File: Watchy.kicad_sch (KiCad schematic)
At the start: 73 parts, among them J1 FPC24(0.5MM), J2 USB_C_Receptacle_USB2.0, J3 Battery, M1 Vibration_Motor, Q1 AO3400A, Q2 UMH3N, Q4 CJ2301, Q5 S8050, SW1 BTN, SW2 BTN, SW3 BTN, SW4 BTN, U1 ESP32-PICO-D4, U2 ME6211C33M5G-N, U3 CP2102, U4 BMA423, U5 TP4054, U6 PCF8563BS, Y1 32.768KHz

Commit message: fix: inconsistent and missing footprints
May have broken something.
Also updated the PCB with the new footprints.
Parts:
- C12, C3, C4: footprint Capacitors_SMD:C_0805 -> Watchy:C_0805
- D1, D2, D3, D4: footprint Diodes_SMD:D_SOD-123 -> Watchy:D_SOD-123
- D5: footprint LEDs:LED_0603 -> Watchy:LED_0603
- D6: footprint Diodes_SMD:D_SOD-123F -> Watchy:D_SOD-123
- L1: footprint Inductors:Inductor_Taiyo-Yuden_NR-40xx -> Inductor_SMD:L_Taiyo-Yuden_NR-40xx
- Q1, Q4, Q5: footprint TO_SOT_Packages_SMD:SOT-23 -> Watchy:SOT-23
- Q2: footprint TO_SOT_Packages_SMD:SOT-363_SC-70-6 -> Package_TO_SOT_SMD:SOT-363_SC-70-6
- R1, R10, R12, R13, R14, R15, R16, R17, R2, R3, R4, R5, R6, R7, R8, R9: footprint Resistors_SMD:R_0402 -> Watchy:R_0402
- U1: footprint Housings_DFN_QFN:QFN-48-1EP_7x7mm_Pitch0.5mm -> Package_DFN_QFN:QFN-48-1EP_7x7mm_P0.5mm_EP5.15x5.15mm
- U2: footprint TO_SOT_Packages_SMD:SOT-23-5 -> Watchy:SOT-23-5
- U4: footprint Housings_LGA:LGA-12_2x2mm_Pitch0.5mm -> Package_LGA:LGA-12_2x2mm_P0.5mm
- U5: footprint TO_SOT_Packages_SMD:SOT-23-5 -> Package_TO_SOT_SMD:SOT-23-5
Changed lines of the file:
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@@
       (effects (font (size 1.27 1.27)))
     )
-    (property "Footprint" "Resistors_SMD:R_0402" (at 17.399 20.574 90)
+    (property "Footprint" "Watchy:R_0402" (at 17.399 20.574 90)
       (effects (font (size 1.27 1.27)) hide)
     )
@@
       (effects (font (size 1.27 1.27)))
     )
-    (property "Footprint" "Resistors_SMD:R_0402" (at 85.09 122.174 90)
+    (property "Footprint" "Watchy:R_0402" (at 85.09 122.174 90)
       (effects (font (size 1.27 1.27)) hide)
     )
@@
       (effects (font (size 1.27 1.27)))
     )
-    (property "Footprint" "Resistors_SMD:R_0402" (at 85.09 129.794 90)
+    (property "Footprint" "Watchy:R_0402" (at 85.09 129.794 90)
       (effects (font (size 1.27 1.27)) hide)
     )
@@
       (effects (font (size 1.27 1.27)) (justify left))
     )
-    (property "Footprint" "TO_SOT_Packages_SMD:SOT-23-5" (at 51.562 113.284 0)
+    (property "Footprint" "Watchy:SOT-23-5" (at 51.562 113.284 0)
       (effects (font (size 1.27 1.27) italic) hide)
     )
@@
       (effects (font (size 1.27 1.27)) (justify left))
     )
-    (property "Footprint" "TO_SOT_Packages_SMD:SOT-23" (at 30.734 116.459 0)
+    (property "Footprint" "Watchy:SOT-23" (at 30.734 116.459 0)
       (effects (font (size 1.27 1.27) italic) (justify left) hide)
     )
@@
       (effects (font (size 1.27 1.27)))
     )
-    (property "Footprint" "Resistors_SMD:R_0402" (at 27.051 130.429 90)
+    (property "Footprint" "Watchy:R_0402" (at 27.051 130.429 90)
       (effects (font (size 1.27 1.27)) hide)
     )
@@
       (effects (font (size 1.27 1.27)))
     )
-    (property "Footprint" "Diodes_SMD:D_SOD-123" (at 32.639 126.619 0)
+    (property "Footprint" "Watchy:D_SOD-123" (at 32.639 126.619 0)
       (effects (font (size 1.27 1.27)) hide)
     )
@@
       (effects (font (size 1.27 1.27)) (justify left))
     )
-    (property "Footprint" "Capacitors_SMD:C_0805" (at 65.9892 134.112 0)
-      (effects (font (size 1.27 1.27)) hide)
-    )
-    (property "Datasheet" "" (at 65.024 130.302 0)
+    (property "Footprint" "Watchy:C_0805" (at 65.9892 134.112 0)
+      (effects (font (size 1.27 1.27)) hide)
+    )
+    (property "Datasheet" "~" (at 65.024 130.302 0)
       (effects (font (size 1.27 1.27)) hide)
     )
@@
       (effects (font (size 1.524 1.524)))
     )
-    (property "Footprint" "TO_SOT_Packages_SMD:SOT-23-5" (at 23.876 157.48 0)
+    (property "Footprint" "Package_TO_SOT_SMD:SOT-23-5" (at 23.876 157.48 0)
       (effects (font (size 1.524 1.524)) hide)
     )
@@
       (effects (font (size 1.27 1.27)))
     )
-    (property "Footprint" "Resistors_SMD:R_0402" (at 42.164 153.797 90)
+    (property "Footprint" "Watchy:R_0402" (at 42.164 153.797 90)
       (effects (font (size 1.27 1.27)) hide)
     )
@@
       (effects (font (size 1.27 1.27)))
     )
-    (property "Footprint" "LEDs:LED_0603" (at 46.482 151.765 0)
-      (effects (font (size 1.27 1.27)) hide)
-    )
-    (property "Datasheet" "" (at 46.482 151.765 0)
+    (property "Footprint" "Watchy:LED_0603" (at 46.482 151.765 0)
+      (effects (font (size 1.27 1.27)) hide)
+    )
+    (property "Datasheet" "~" (at 46.482 151.765 0)
       (effects (font (size 1.27 1.27)) hide)
     )
@@
       (effects (font (size 1.27 1.27)))
     )
-    (property "Footprint" "Resistors_SMD:R_0402" (at 19.304 159.385 90)
+    (property "Footprint" "Watchy:R_0402" (at 19.304 159.385 90)
       (effects (font (size 1.27 1.27)) hide)
     )
@@
       (effects (font (size 1.27 1.27)) (justify left))
     )
-    (property "Footprint" "Resistors_SMD:R_0402" (at 142.621 32.512 90)
+    (property "Footprint" "Watchy:R_0402" (at 142.621 32.512 90)
       (effects (font (size 1.27 1.27)) hide)
     )
@@
       (effects (font (size 1.27 1.27)) (justify left))
     )
-    (property "Footprint" "Resistors_SMD:R_0402" (at 142.621 50.292 90)
+    (property "Footprint" "Watchy:R_0402" (at 142.621 50.292 90)
       (effects (font (size 1.27 1.27)) hide)
     )
@@
       (effects (font (size 1.27 1.27)) (justify left))
     )
-    (property "Footprint" "Resistors_SMD:R_0402" (at 142.621 68.072 90)
+    (property "Footprint" "Watchy:R_0402" (at 142.621 68.072 90)
       (effects (font (size 1.27 1.27)) hide)
     )
@@
       (effects (font (size 1.27 1.27)) (justify left))
     )
-    (property "Footprint" "Resistors_SMD:R_0402" (at 142.621 85.852 90)
+    (property "Footprint" "Watchy:R_0402" (at 142.621 85.852 90)
       (effects (font (size 1.27 1.27)) hide)
     )
@@
       (effects (font (size 1.27 1.27)) (justify left))
     )
-    (property "Footprint" "Resistors_SMD:R_0402" (at 93.599 23.241 90)
+    (property "Footprint" "Watchy:R_0402" (at 93.599 23.241 90)
       (effects (font (size 1.27 1.27)) hide)
     )
@@
       (effects (font (size 1.27 1.27)) (justify left))
     )
-    (property "Footprint" "Resistors_SMD:R_0402" (at 99.06 23.241 90)
+    (property "Footprint" "Watchy:R_0402" (at 99.06 23.241 90)
       (effects (font (size 1.27 1.27)) hide)
     )
@@
       (effects (font (size 1.27 1.27)) (justify left))
     )
-    (property "Footprint" "TO_SOT_Packages_SMD:SOT-23" (at 145.669 184.658 0)
+    (property "Footprint" "Watchy:SOT-23" (at 145.669 184.658 0)
       (effects (font (size 1.27 1.27)) hide)
     )
@@
       (effects (font (size 1.27 1.27)) (justify left))
     )
-    (property "Footprint" "Resistors_SMD:R_0402" (at 131.699 185.42 90)
+    (property "Footprint" "Watchy:R_0402" (at 131.699 185.42 90)
       (effects (font (size 1.27 1.27)) hide)
     )
@@
       (effects (font (size 1.27 1.27)) (justify left))
     )
-    (property "Footprint" "Diodes_SMD:D_SOD-123F" (at 138.684 178.308 0)
+    (property "Footprint" "Watchy:D_SOD-123" (at 138.684 178.308 0)
       (effects (font (size 1.27 1.27)) hide)
     )
@@
       (effects (font (size 1.27 1.27)))
     )
-    (property "Footprint" "Housings_DFN_QFN:QFN-48-1EP_7x7mm_Pitch0.5mm" (at 54.61 106.426 0)
+    (property "Footprint" "Package_DFN_QFN:QFN-48-1EP_7x7mm_P0.5mm_EP5.15x5.15mm" (at 54.61 106.426 0)
       (effects (font (size 1.27 1.27)) hide)
     )
@@
       (effects (font (size 1.27 1.27)))
     )
-    (property "Footprint" "Housings_LGA:LGA-12_2x2mm_Pitch0.5mm" (at 249.682 140.081 0)
+    (property "Footprint" "Package_LGA:LGA-12_2x2mm_P0.5mm" (at 249.682 140.081 0)
       (effects (font (size 1.27 1.27)) (justify left bottom) hide)
     )
@@
       (effects (font (size 1.27 1.27)) (justify left))
     )
-    (property "Footprint" "Capacitors_SMD:C_0805" (at 184.0992 56.388 0)
+    (property "Footprint" "Watchy:C_0805" (at 184.0992 56.388 0)
       (effects (font (size 1.27 1.27)) hide)
     )
@@
       (effects (font (size 1.27 1.27)))
     )
-    (property "Footprint" "Inductors:Inductor_Taiyo-Yuden_NR-40xx" (at 186.944 48.768 0)
+    (property "Footprint" "Inductor_SMD:L_Taiyo-Yuden_NR-40xx" (at 186.944 48.768 0)
       (effects (font (size 1.27 1.27)) hide)
     )
@@
       (effects (font (size 1.27 1.27)) (justify left))
     )
-    (property "Footprint" "Capacitors_SMD:C_0805" (at 191.7192 48.768 0)
+    (property "Footprint" "Watchy:C_0805" (at 191.7192 48.768 0)
       (effects (font (size 1.27 1.27)) hide)
     )
@@
       (effects (font (size 1.27 1.27)))
     )
-    (property "Footprint" "Diodes_SMD:D_SOD-123" (at 194.564 37.973 0)
+    (property "Footprint" "Watchy:D_SOD-123" (at 194.564 37.973 0)
       (effects (font (size 1.27 1.27)) hide)
     )
@@
       (effects (font (size 1.27 1.27)))
     )
-    (property "Footprint" "Diodes_SMD:D_SOD-123" (at 194.564 41.148 0)
+    (property "Footprint" "Watchy:D_SOD-123" (at 194.564 41.148 0)
       (effects (font (size 1.27 1.27)) hide)
     )
@@
       (effects (font (size 1.27 1.27)))
     )
-    (property "Footprint" "Diodes_SMD:D_SOD-123" (at 194.564 48.768 0)
+    (property "Footprint" "Watchy:D_SOD-123" (at 194.564 48.768 0)
       (effects (font (size 1.27 1.27)) hide)
     )
@@
       (effects (font (size 1.27 1.27)) (justify left))
     )
-    (property "Footprint" "TO_SOT_Packages_SMD:SOT-23" (at 193.294 72.39 0)
+    (property "Footprint" "Watchy:SOT-23" (at 193.294 72.39 0)
       (effects (font (size 1.27 1.27) italic) (justify left) hide)
     )
@@
       (effects (font (size 1.27 1.27)) (justify left))
     )
-    (property "Footprint" "Resistors_SMD:R_0402" (at 181.356 74.295 90)
+    (property "Footprint" "Watchy:R_0402" (at 181.356 74.295 90)
       (effects (font (size 1.27 1.27)) hide)
     )
@@
       (effects (font (size 1.27 1.27)) (justify left))
     )
-    (property "Footprint" "Resistors_SMD:R_0402" (at 194.564 73.787 90)
+    (property "Footprint" "Watchy:R_0402" (at 194.564 73.787 90)
       (effects (font (size 1.27 1.27)) hide)
     )
@@
       (effects (font (size 1.27 1.27)) (justify left))
     )
-    (property "Footprint" "Resistors_SMD:R_0402" (at 51.054 184.15 90)
+    (property "Footprint" "Watchy:R_0402" (at 51.054 184.15 90)
       (effects (font (size 1.27 1.27)) hide)
     )
@@
       (effects (font (size 1.27 1.27)) (justify left))
     )
-    (property "Footprint" "TO_SOT_Packages_SMD:SOT-363_SC-70-6" (at 29.083 81.28 0)
+    (property "Footprint" "Package_TO_SOT_SMD:SOT-363_SC-70-6" (at 29.083 81.28 0)
       (effects (font (size 1.27 1.27)) hide)
     )
@@
       (effects (font (size 1.27 1.27)) (justify left))
     )
-    (property "Footprint" "TO_SOT_Packages_SMD:SOT-363_SC-70-6" (at 29.083 96.647 0)
-      (effects (font (size 1.27 1.27)) hide)
-    )
+    (property "Footprint" "Package_TO_SOT_SMD:SOT-363_SC-70-6" (at 29.083 96.647 0)
+      (effects (font (size 1.27 1.27)) hide)
+    )

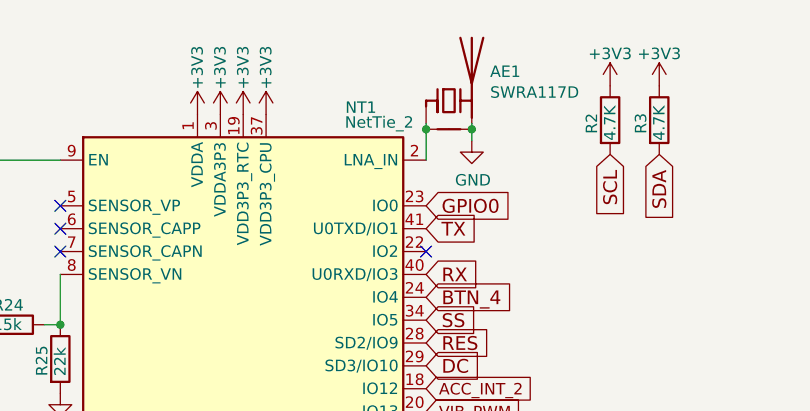
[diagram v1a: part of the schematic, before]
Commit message: remove net tie
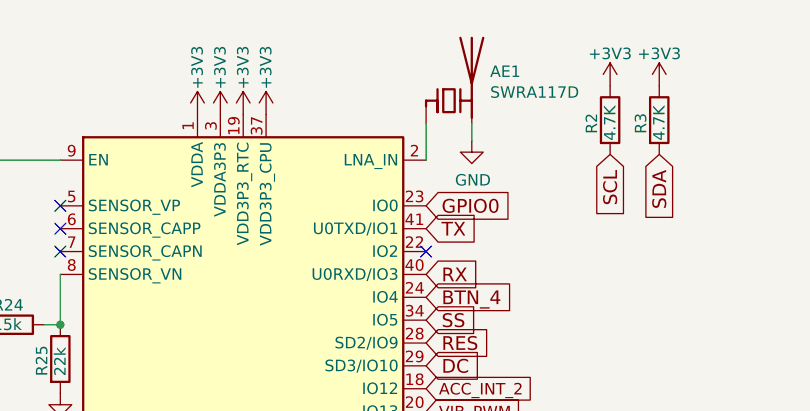
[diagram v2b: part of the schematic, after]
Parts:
- removed NT1: NetTie_2, symbol Device:NetTie_2
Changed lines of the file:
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@@
   (junction (at 68.58 180.848) (diameter 0) (color 0 0 0 0)
   )
-  (junction (at 80.01 24.257) (diameter 0) (color 0 0 0 0)
-  )
   (junction (at 40.513 118.999) (diameter 0) (color 0 0 0 0)
   )
@@
   (junction (at 19.177 27.686) (diameter 0) (color 0 0 0 0)
   )
-  (junction (at 74.93 24.257) (diameter 0) (color 0 0 0 0)
-  )
   (junction (at 151.765 128.651) (diameter 0) (color 0 0 0 0)
   )
@@
     (stroke (width 0) (type default))
   )
-  (wire (pts (xy 80.01 24.257) (xy 80.01 23.622))
+  (wire (pts (xy 80.01 23.622) (xy 80.01 25.527))
     (stroke (width 0) (type default))
   )
@@
     (stroke (width 0) (type default))
   )
-  (wire (pts (xy 74.93 24.257) (xy 74.93 23.622))
+  (wire (pts (xy 74.93 23.622) (xy 74.93 27.686))
     (stroke (width 0) (type default))
   )
@@
     (stroke (width 0) (type default))
   )
-  (wire (pts (xy 74.93 27.686) (xy 74.93 24.257))
-    (stroke (width 0) (type default))
-  )
   (wire (pts (xy 190.754 48.768) (xy 190.754 65.405))
     (stroke (width 0) (type default))
@@
     (stroke (width 0) (type default))
   )
-  (wire (pts (xy 80.01 25.527) (xy 80.01 24.257))
-    (stroke (width 0) (type default))
-  )
   (wire (pts (xy 75.184 180.848) (xy 68.58 180.848))
     (stroke (width 0) (type default))
@@
         )
       )
-    )
-  )
-  (symbol (lib_id "Device:NetTie_2") (at 77.47 24.257 0) (unit 1)
-    (in_bom no) (on_board yes) (dnp no)
-    (property "Reference" "NT1" (at 67.691 21.844 0)
-      (effects (font (size 1.27 1.27)))
-    )
-    (property "Value" "NetTie_2" (at 69.723 23.495 0)
-      (effects (font (size 1.27 1.27)))
-    )
-    (property "Footprint" "" (at 77.47 24.257 0)
-      (effects (font (size 1.27 1.27)) hide)
-    )
-    (property "Datasheet" "~" (at 77.47 24.257 0)
-      (effects (font (size 1.27 1.27)) hide)
-    )
-    (pin "1")
-    (pin "2")
-    (instances
-      (project "Watchy"
-        (path "/4168ccf9-7940-46a9-babd-bad8c703bb50"
-          (reference "NT1") (unit 1)
-        )
-      )

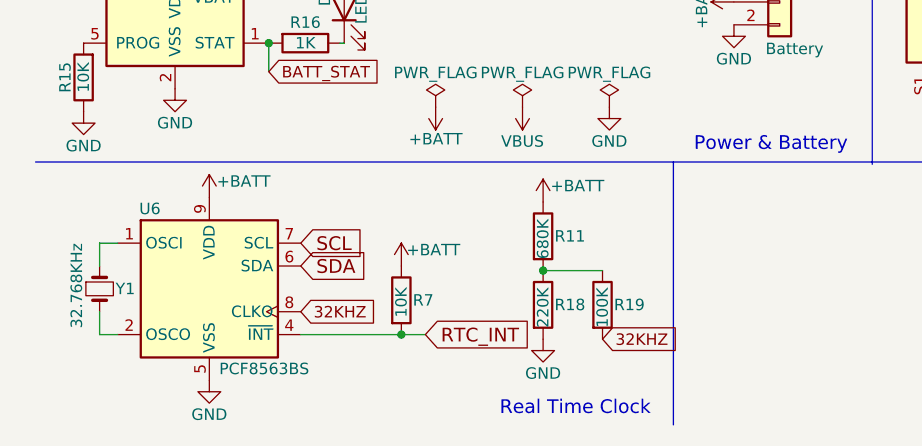
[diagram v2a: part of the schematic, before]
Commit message: update schematic for trim capacitor
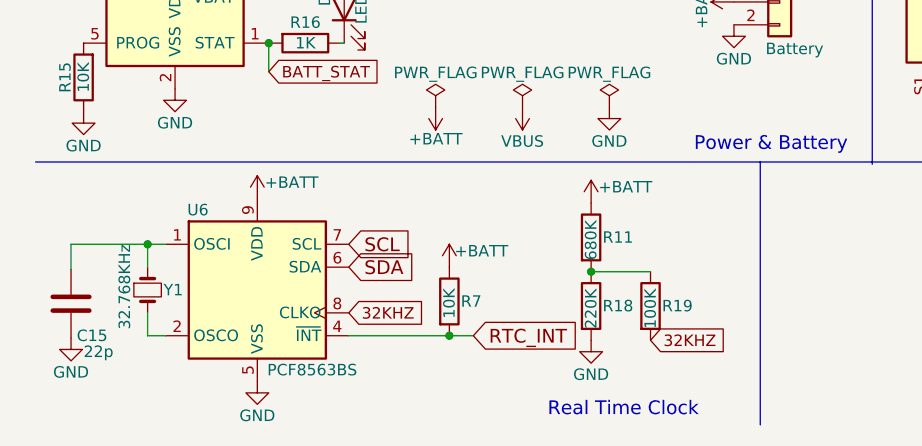
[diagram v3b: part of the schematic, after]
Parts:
- added C15: 22p, Capacitor_SMD:C_0603_1608Metric, symbol Device:C
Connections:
- net GND: now also C15.2
- net at U6.1 (OSCI), Y1.1: now also C15.1
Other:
- moved on the sheet: R11, R18, R19, R7, U6, Y1

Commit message: Revert "update schematic for trim capacitor"
This reverts commit bc47ff4912a5bf578d20c0e57acb1b5880a0f2bb.
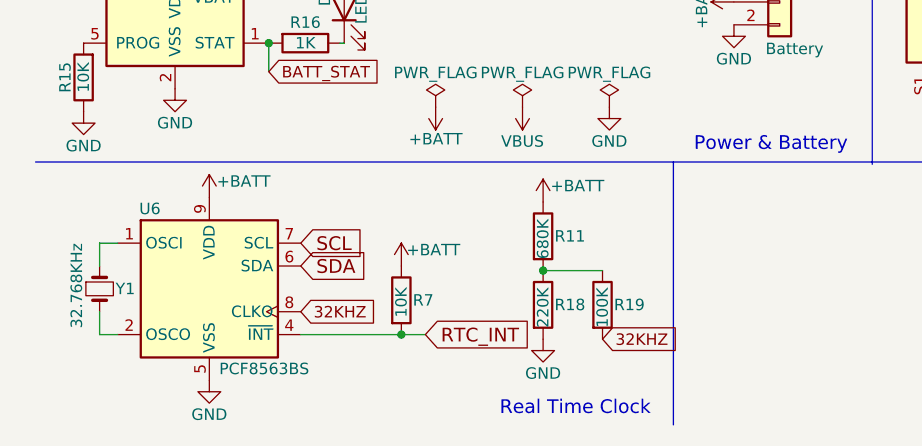
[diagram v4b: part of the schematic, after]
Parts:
- removed C15: 22p, Capacitor_SMD:C_0603_1608Metric, symbol Device:C
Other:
- moved on the sheet: R11, R18, R19, R7, U6, Y1

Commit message: also save schematic
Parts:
- removed J3: Battery, Watchy:1.25T-2PWT (Molex 532610271), symbol Connector_Generic:Conn_01x02
- added C15: 22pF, Capacitor_SMD:C_0603_1608Metric, symbol Device:C
- added J4, J5: Conn_01x01, Watchy:BatteryPads, symbol Connector_Generic:Conn_01x01
- C1: value 100nF -> 1uF/50V
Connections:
- net +BATT: now also J4.1 (Pin_1)
- net GND: now also C15.2, J5.1 (Pin_1)
- net at U6.1 (OSCI), Y1.1: now also C15.1
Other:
- moved on the sheet: R11, R18, R19, R7, U6, Y1
